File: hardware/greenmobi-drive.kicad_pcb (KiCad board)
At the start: 2 copper layers, 100 x 100 mm, 160 parts, among them J101 UBAT, J102 GND, J103 Encoder/Hall, J104 Motor NTC, J105 USB_C_Receptacle_USB2.0_14P, J106 CAN, J107 ADC, J108 ADC, J201 Debug, J301 Phase_OUT, J401 Phase_OUT, J501 Phase_OUT, Q301 IPT015N10N5, Q302 IPT015N10N5, Q401 IPT015N10N5, Q402 IPT015N10N5, Q501 IPT015N10N5, Q502 IPT015N10N5, U101 BMI323, U102 TJA1051T-3, U201 STM32F405RGTx, U301 IRS21867S, U302 INA240A2D, U401 IRS21867S, U402 INA240A2D, U501 IRS21867S, U502 INA240A2D, U601 TPS54202DDC, U602 LM5163DDA, U603 AMS1117-3.3, Y201 8MHz

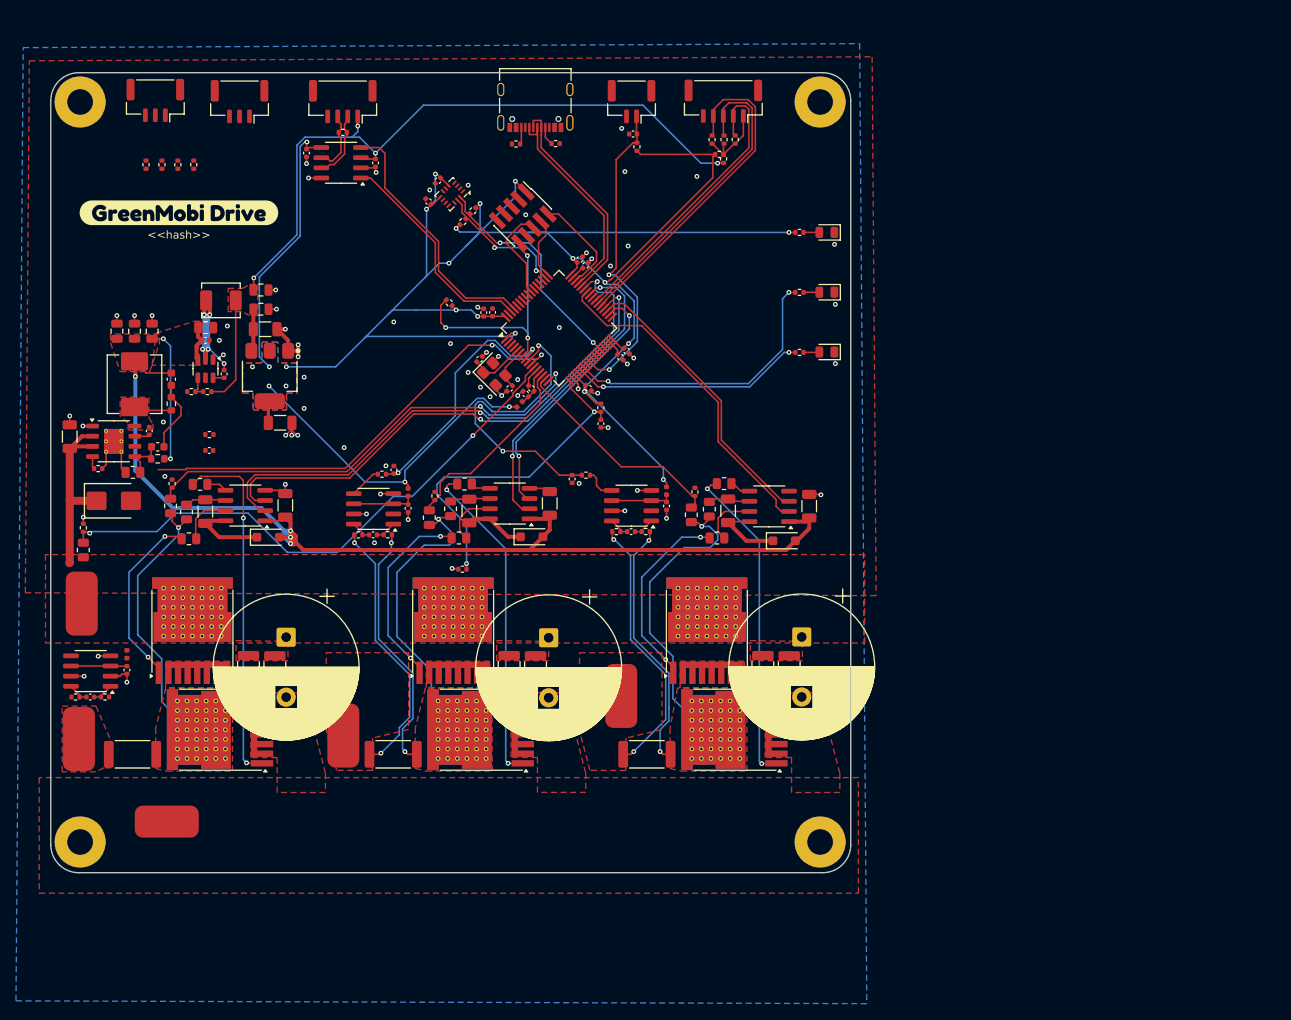
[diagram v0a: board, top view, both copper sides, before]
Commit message: Reduce board size
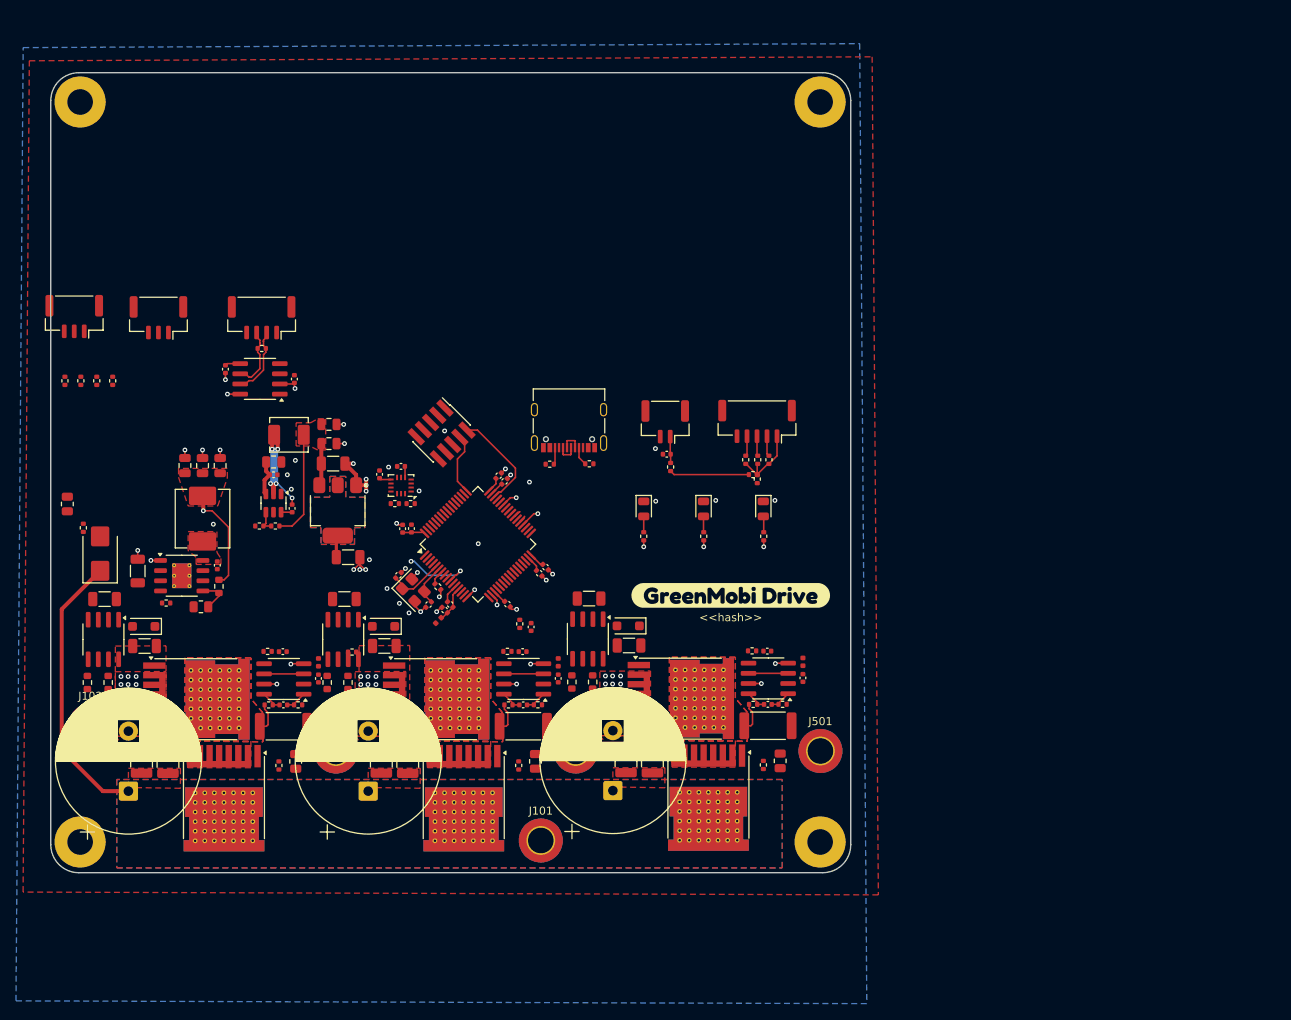
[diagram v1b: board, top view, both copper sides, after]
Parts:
- removed C608: 56p, Capacitor_SMD:C_0603_1608Metric
- removed C609: 3.3n, Capacitor_SMD:C_0603_1608Metric
- removed R301, R401, R501: 0, Resistor_SMD:R_0805_2012Metric
- removed R604: 453k, Resistor_SMD:R_0603_1608Metric
- J101, J102, J301, J401, J501: footprint Connector_Wire:SolderWirePad_1x01_SMD_4x8mm -> MountingHole:MountingHole_3.2mm_M3_ISO14580_Pad_TopBottom
- R308, R309, R408, R409, R508, R509: footprint Resistor_SMD:R_0805_2012Metric -> Resistor_SMD:R_0603_1608Metric
- moved J501 92.7 mm to (190.1, 130.8), turned to 0 degrees
- moved R507 84.7 mm to (185.4, 125.0)
- moved U502 84.7 mm to (183.6, 121.8)
- moved C505 84.7 mm to (183.6, 125.0)
- moved R505 84.7 mm to (181.7, 125.0)
- moved C504 84.5 mm to (187.9, 121.7)
- moved L501 84.5 mm to (187.9, 119.7)
- moved kibuzzard-6884DDAB 83.9 mm to (178.9, 111.4)
- moved R502 82.6 mm to (185.1, 132.1)
- moved R503 81.8 mm to (183.0, 132.6)
- moved R506 79.5 mm to (183.6, 127.7), turned to 0 degrees
- moved C503 74.1 mm to (183.5, 118.3)
- moved R504 73.0 mm to (181.6, 118.3), turned to 180 degrees
- moved Q501 67.8 mm to (176.1, 136.7), turned to -90 degrees
- moved J101 64.6 mm to (155.2, 142.0)
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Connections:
- C302 pad 2: Net-(U301-VS) -> Net-(Q301-S)
- C402 pad 2: Net-(U401-VS) -> Net-(Q401-S)
- C502 pad 2: Net-(U501-VS) -> Net-(Q501-S)
- U301 pad 6: Net-(U301-VS) -> Net-(Q301-S)
- U401 pad 6: Net-(U401-VS) -> Net-(Q401-S)
- U501 pad 6: Net-(U501-VS) -> Net-(Q501-S)
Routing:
- net +3.3V: track 315.1 -> 27.8 mm, vias 23 -> 2
- net (no net): track 240.3 -> 0.00 mm, vias 11 -> 0
- net +12V: track 157.1 -> 17.9 mm, vias 6 -> 1
- net +5V: track 105.2 -> 18.9 mm, vias 4 -> 0
- net /mcu/Vin: track 70.9 -> 0.00 mm, vias 2 -> 0
- net /half-bridge2/HIGH: track 69.4 -> 2.04 mm, vias 2 -> 1
- net /half-bridge2/LOW: track 64.9 -> 2.46 mm, vias 2 -> 1
- net /half-bridge2/Phase_V: track 58.3 -> 1.37 mm, vias 2 -> 1
- net /half-bridge2/Current_sense: track 57.1 -> 8.95 mm
- net Net-(Q502-G): track 44.4 -> 0.00 mm, vias 2 -> 0
- net /mcu/MOS_TEMP: track 42.4 -> 0.00 mm, vias 2 -> 0
- net /half-bridge1/HIGH: track 41.5 -> 0.00 mm
- net Net-(Q302-G): track 41.1 -> 0.00 mm, vias 2 -> 0
- net Net-(Q402-G): track 40.5 -> 0.00 mm, vias 2 -> 0
- net /half-bridge/HIGH: track 39.0 -> 0.00 mm, vias 2 -> 0
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- added copper zone on B.Cu, net /Regulators/BAT
- removed copper zone on F.Cu, net Net-(J301-Pin_1)
- removed copper zone on F.Cu, net Net-(J401-Pin_1)
- removed copper zone on F.Cu, net Net-(J501-Pin_1)

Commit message: Test fit on 50x100mm
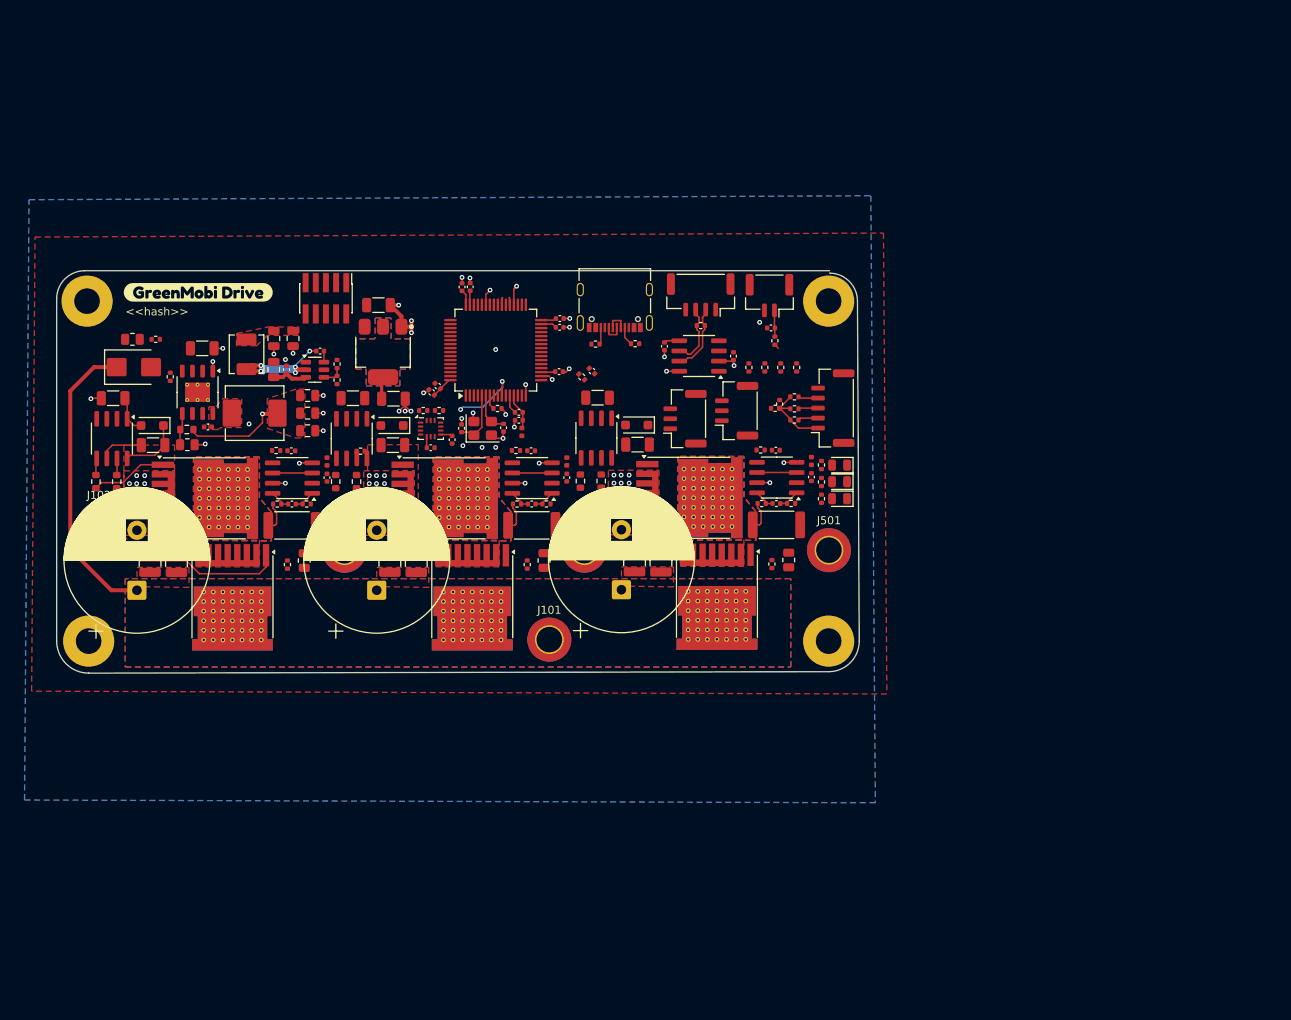
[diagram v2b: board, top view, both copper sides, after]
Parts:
- removed kibuzzard-6884DDAB: G***, kibuzzard-6884DDAB
- added kibuzzard-68C86CBD: G***, kibuzzard-68C86CBD, F.Cu at (112.4, 73.5)
- moved R117 85.5 mm to (183.2, 82.9)
- moved R116 85.5 mm to (181.2, 82.9)
- moved R119 85.5 mm to (187.2, 82.9)
- moved R118 85.5 mm to (185.2, 82.9)
- moved J107 83.6 mm to (179.7, 88.3), turned to 90 degrees
- moved J108 67.0 mm to (173.2, 89.3), turned to 90 degrees
- moved R115 55.0 mm to (175.2, 77.6)
- moved C105 55.0 mm to (170.6, 80.2)
- moved J106 55.0 mm to (175.2, 73.8)
- moved U102 55.0 mm to (175.0, 81.5)
- moved C106 55.0 mm to (179.3, 81.5)
- moved C104 32.9 mm to (161.6, 83.3), turned to -45 degrees
- moved R112 31.8 mm to (160.3, 84.1), turned to -45 degrees
- moved C212 31.1 mm to (157.6, 76.8), turned to 0 degrees
- moved C205 30.8 mm to (157.5, 77.9), turned to 0 degrees
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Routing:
- net Net-(Q301-G): track 0.00 -> 28.5 mm
- net +5V: track 18.9 -> 0.00 mm
- net /mcu/SWIO: track 12.8 -> 0.00 mm
- net +3.3V: track 27.8 -> 17.6 mm, vias 2 -> 1
- net Net-(Q302-G): track 0.00 -> 9.59 mm
- net Net-(D301-K): track 0.00 -> 7.93 mm
- net /mcu/SWCLK: track 7.82 -> 0.00 mm
- net Net-(Q301-S): track 3.77 -> 9.33 mm
- net +12V: track 17.9 -> 22.2 mm
- net GND: track 49.0 -> 51.7 mm, vias 105 -> 96
- net /Regulators/BAT: track 34.9 -> 37.3 mm
- net /half-bridge/LS: track 0.00 -> 2.11 mm
- net /half-bridge/HS: track 0.00 -> 2.09 mm
- net Net-(D102-A): track 2.00 -> 0.00 mm
- net Net-(D103-A): track 1.99 -> 0.00 mm
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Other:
- board size 100 x 100 mm -> 100.3 x 50.3 mm

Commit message: Changed bootstrap diode and gate resistor
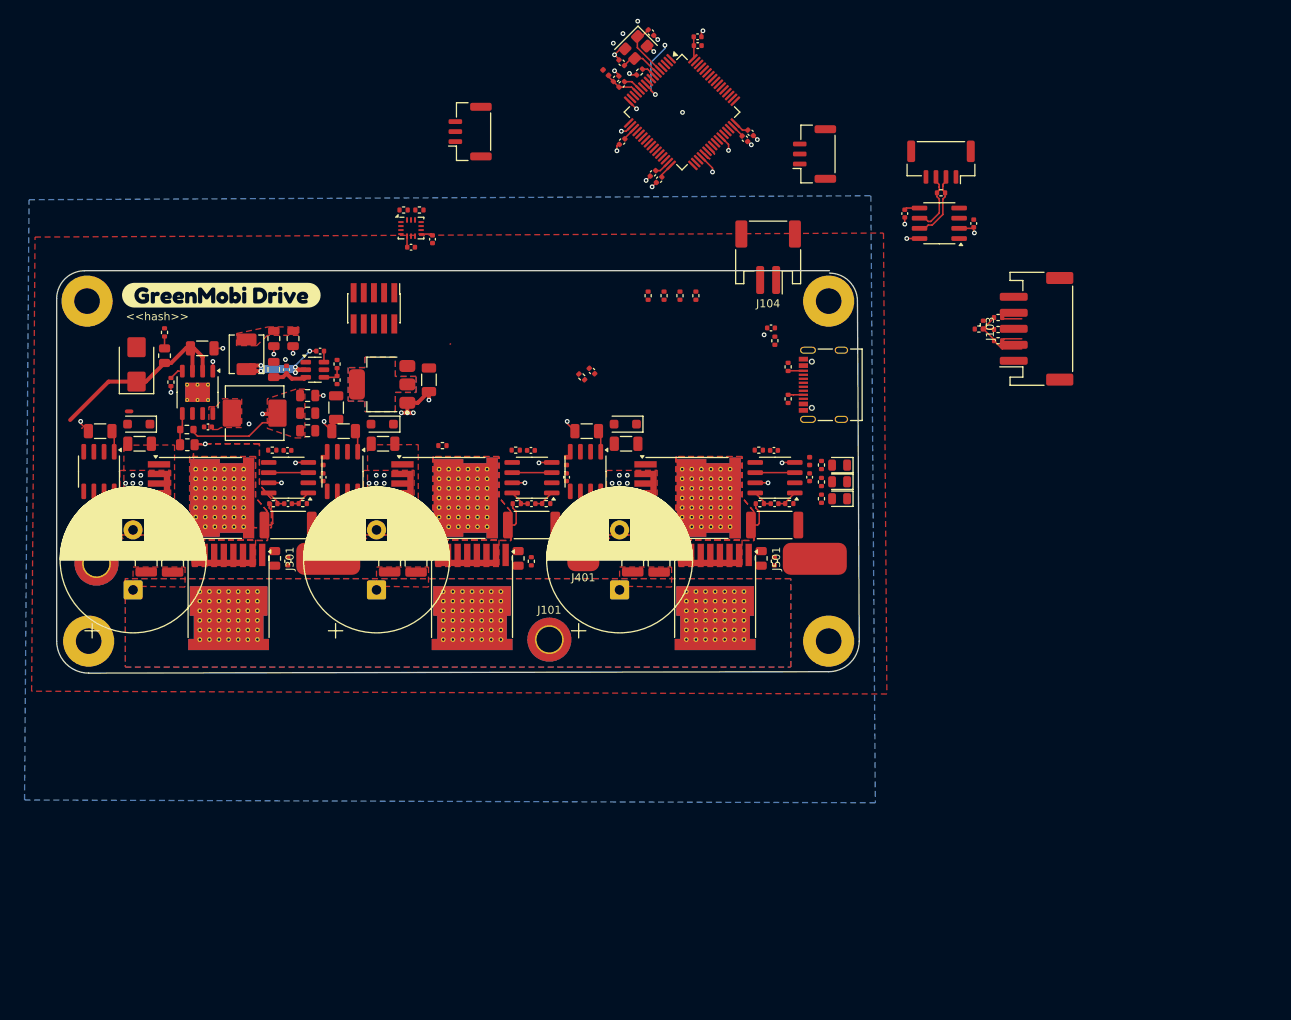
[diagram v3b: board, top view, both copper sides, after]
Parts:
- removed kibuzzard-68C86CBD: G***, kibuzzard-68C86CBD
- added kibuzzard-68C90E22: G***, kibuzzard-68C90E22, F.Cu at (115.2, 73.8)
- D301, D401, D501: value PMEG2010EH -> PMEG6010CEH
- J103: footprint Connector_JST:JST_GH_SM05B-GHS-TB_1x05-1MP_P1.25mm_Horizontal -> Connector_JST:JST_PH_S5B-PH-SM4-TB_1x05-1MP_P2.00mm_Horizontal
- J104: footprint Connector_JST:JST_GH_SM02B-GHS-TB_1x02-1MP_P1.25mm_Horizontal -> Connector_JST:JST_PH_S2B-PH-SM4-TB_1x02-1MP_P2.00mm_Horizontal
- J301, J401, J501: footprint MountingHole:MountingHole_3.2mm_M3_ISO14580_Pad_TopBottom -> Connector_Wire:SolderWirePad_1x01_SMD_4x8mm
- R308, R309, R408, R409, R508, R509: value 10 -> 4.7
- moved C209 55.5 mm to (174.8, 41.5), turned to 0 degrees
- moved C203 54.8 mm to (169.0, 41.0), turned to -45 degrees
- moved C210 53.5 mm to (174.8, 42.6), turned to 0 degrees
- moved Y201 51.3 mm to (167.1, 42.9), turned to -135 degrees
- moved C204 48.0 mm to (165.3, 44.8), turned to 135 degrees
- moved L201 46.1 mm to (163.3, 46.0), turned to -45 degrees
- moved R201 45.7 mm to (167.5, 46.0), turned to 45 degrees
- moved J108 44.8 mm to (146.3, 53.4)
- moved C208 44.4 mm to (164.6, 46.8), turned to 45 degrees
- moved C206 43.0 mm to (165.3, 47.5), turned to 45 degrees
- moved C211 40.9 mm to (181.4, 53.5), turned to -45 degrees
- moved C207 39.0 mm to (180.7, 54.3), turned to -45 degrees
- moved U201 37.8 mm to (172.8, 51.0), turned to -45 degrees
- moved C106 34.3 mm to (209.3, 64.9)
- moved J106 34.3 mm to (205.2, 57.2)
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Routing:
- net Net-(Q301-G): track 28.5 -> 0.00 mm
- net /Regulators/BAT: track 37.3 -> 25.5 mm
- net Net-(Q302-G): track 9.59 -> 0.00 mm
- net Net-(D301-K): track 7.93 -> 0.00 mm
- net Net-(Q301-S): track 9.33 -> 3.77 mm
- net +12V: track 22.2 -> 27.3 mm
- net GND: track 51.7 -> 48.0 mm, vias 96 -> 92
- net +3.3V: track 17.6 -> 14.2 mm
- net /mcu/TEMP_MOTOR: track 3.31 -> 0.00 mm
- net /Interfaces/USB_DP: track 2.70 -> 0.00 mm
- net /Interfaces/USB_DN: track 2.70 -> 0.00 mm
- net /half-bridge/LS: track 2.11 -> 0.00 mm
- net /half-bridge/HS: track 2.09 -> 0.00 mm
- net Net-(U602-RON): track 0.00 -> 1.78 mm
- net /mcu/Vin: track 0.00 -> 1.49 mm

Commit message: Layout work
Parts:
- J103: footprint Connector_JST:JST_PH_S5B-PH-SM4-TB_1x05-1MP_P2.00mm_Horizontal -> Connector_JST:JST_PH_B5B-PH-SM4-TB_1x05-1MP_P2.00mm_Vertical
- J104: footprint Connector_JST:JST_PH_S2B-PH-SM4-TB_1x02-1MP_P2.00mm_Horizontal -> Connector_JST:JST_PH_B2B-PH-SM4-TB_1x02-1MP_P2.00mm_Vertical
- J106: footprint Connector_JST:JST_GH_SM04B-GHS-TB_1x04-1MP_P1.25mm_Horizontal -> Connector_JST:JST_PH_B4B-PH-SM4-TB_1x04-1MP_P2.00mm_Vertical
- J107, J108: footprint Connector_JST:JST_GH_SM03B-GHS-TB_1x03-1MP_P1.25mm_Horizontal -> Connector_JST:JST_PH_B3B-PH-SM4-TB_1x03-1MP_P2.00mm_Vertical
- moved C213 97.1 mm to (230.3, 126.9), turned to -90 degrees
- moved L201 96.6 mm to (222.8, 122.2), turned to 0 degrees
- moved C208 95.8 mm to (224.2, 121.8), turned to 90 degrees
- moved C206 95.5 mm to (225.2, 121.8), turned to 90 degrees
- moved C205 95.4 mm to (235.8, 126.9), turned to -90 degrees
- moved C212 95.1 mm to (236.9, 126.9), turned to -90 degrees
- moved C204 94.9 mm to (223.3, 119.9), turned to 180 degrees
- moved R201 93.5 mm to (225.7, 119.2), turned to 90 degrees
- moved Y201 93.2 mm to (223.2, 117.3), turned to -90 degrees
- moved C203 91.5 mm to (223.2, 114.7), turned to 0 degrees
- moved U201 90.8 mm to (233.0, 119.0), turned to 0 degrees
- moved C210 87.5 mm to (228.5, 111.7), turned to 45 degrees
- moved C209 87.2 mm to (227.7, 110.9), turned to 45 degrees
- moved C207 86.0 mm to (240.9, 115.7), turned to 0 degrees
- moved C211 85.3 mm to (240.9, 114.7), turned to 0 degrees
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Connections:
- J106 pad 1: +5V -> GND
- J106 pad 2: /Interfaces/CAN_P -> /Interfaces/CAN_N
- J106 pad 3: /Interfaces/CAN_N -> /Interfaces/CAN_P
- J106 pad 4: GND -> +5V
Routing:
- net /Regulators/BAT: track 25.5 -> 10.7 mm
- net GND: track 48.0 -> 43.3 mm, vias 92 -> 90
- net Net-(U602-BST): track 0.00 -> 1.75 mm
- net /mcu/Vin: track 1.49 -> 0.00 mm
- net +12V: track 27.3 -> 26.7 mm
- removed copper zone on F.Cu, net +5V
